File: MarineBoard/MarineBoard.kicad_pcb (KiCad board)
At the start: 4 copper layers, 66.5 x 70 mm, 151 parts, among them CN1 MKDSN 1,5/ 2-5,08, CN2 MKDSN 1,5/ 2-5,08, CN3 SM04B-SRSS-TB (LF)(SN), J1 USB_C_Receptacle_USB2.0_16P, J3 Conn_02x09_Top_Bottom, Q1 IPL60R075CFD7, Q2 S8050, Q3 S8050, U1 SY8089A1AAC, U10 PC817C-S, U11 SN65HVD230DR, U12 DB125-3.5-3P-GN-S, U13 DB125-3.5-3P-GN-S, U14 PC817C-S, U15 TC4427EPA, U16 PC817C-S, U17 PC817C-S, U18 INA226, U19 INA226, U2 INA226, U20 SMAJ6.8CA, U3 TPS5430DDA, U4 DB125-3.5-2P-GN-S, U5 DB125-3.5-2P-GN-S, U6 DB125-3.5-2P-GN-S, U7 DB125-3.5-3P-GN-S, U8 ESP32-S3-WROOM-2-N32R16V, U9 DB125-3.5-3P-GN-S

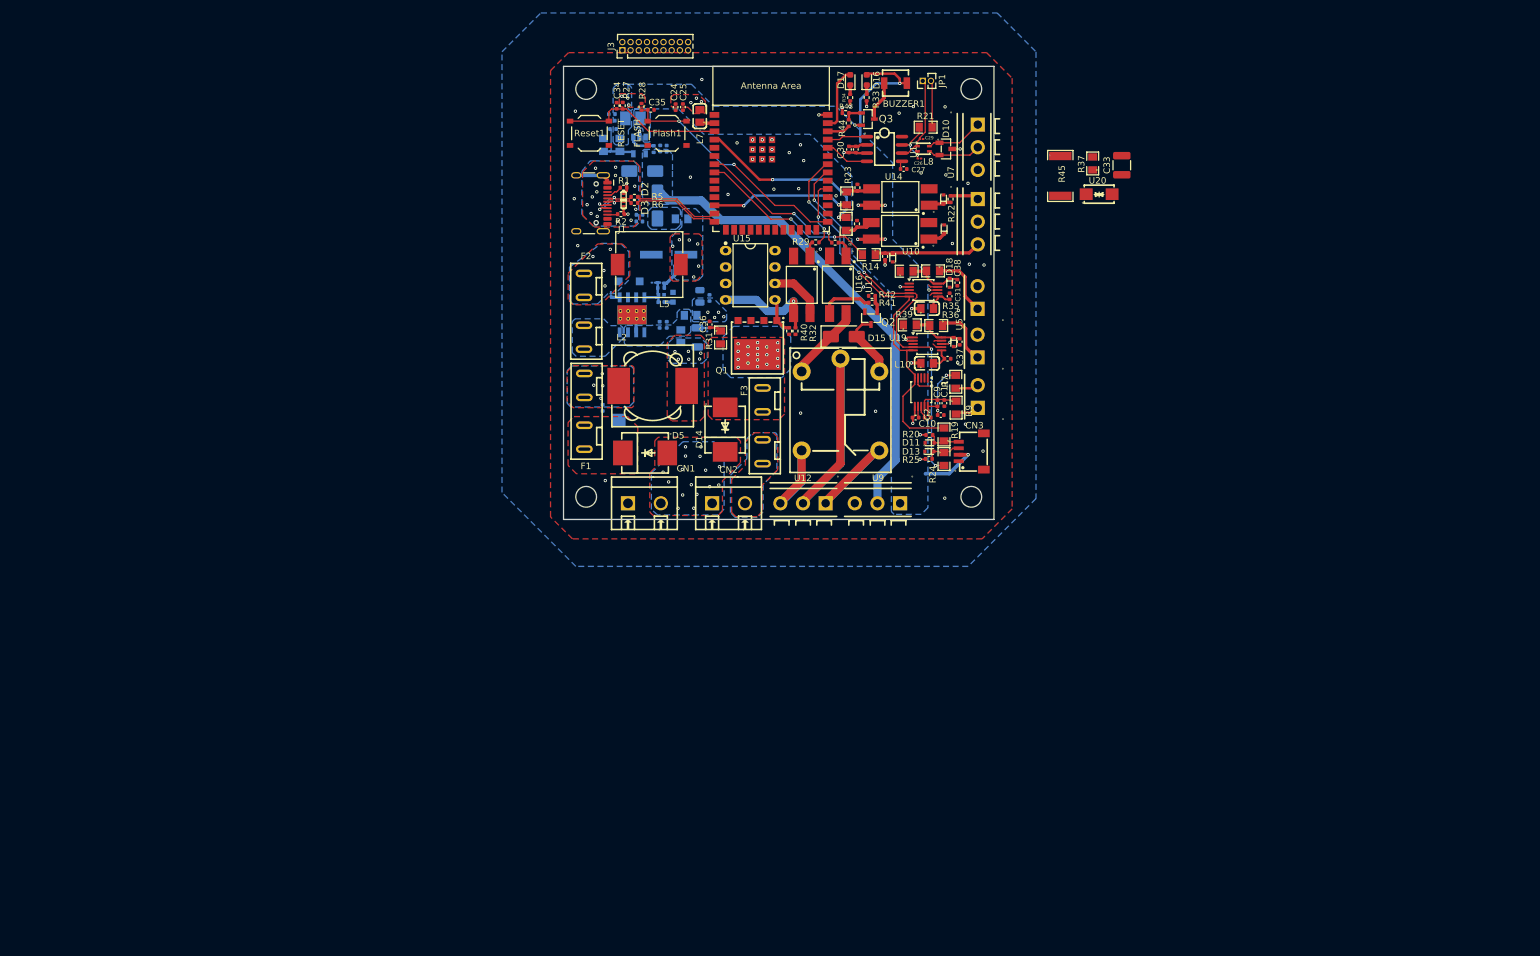
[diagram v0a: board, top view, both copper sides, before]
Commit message: MarineBoard: new from-scratch layout; Quilter-compatible footprints
- LCSC: nickname on all EasyEDA footprint lib IDs (board + schematic)
- EasyEDA.pretty upgraded to current KiCad format; 3D models moved to Lib/Models
- U10 FPC mounting tabs numbered 21/22 to match symbol
- L2 silkscreen arcs replaced with line segments (Quilter parser rejects fp_arc)

Co-Authored-By: Claude Opus 5.5 <noreply@anthropic.com>
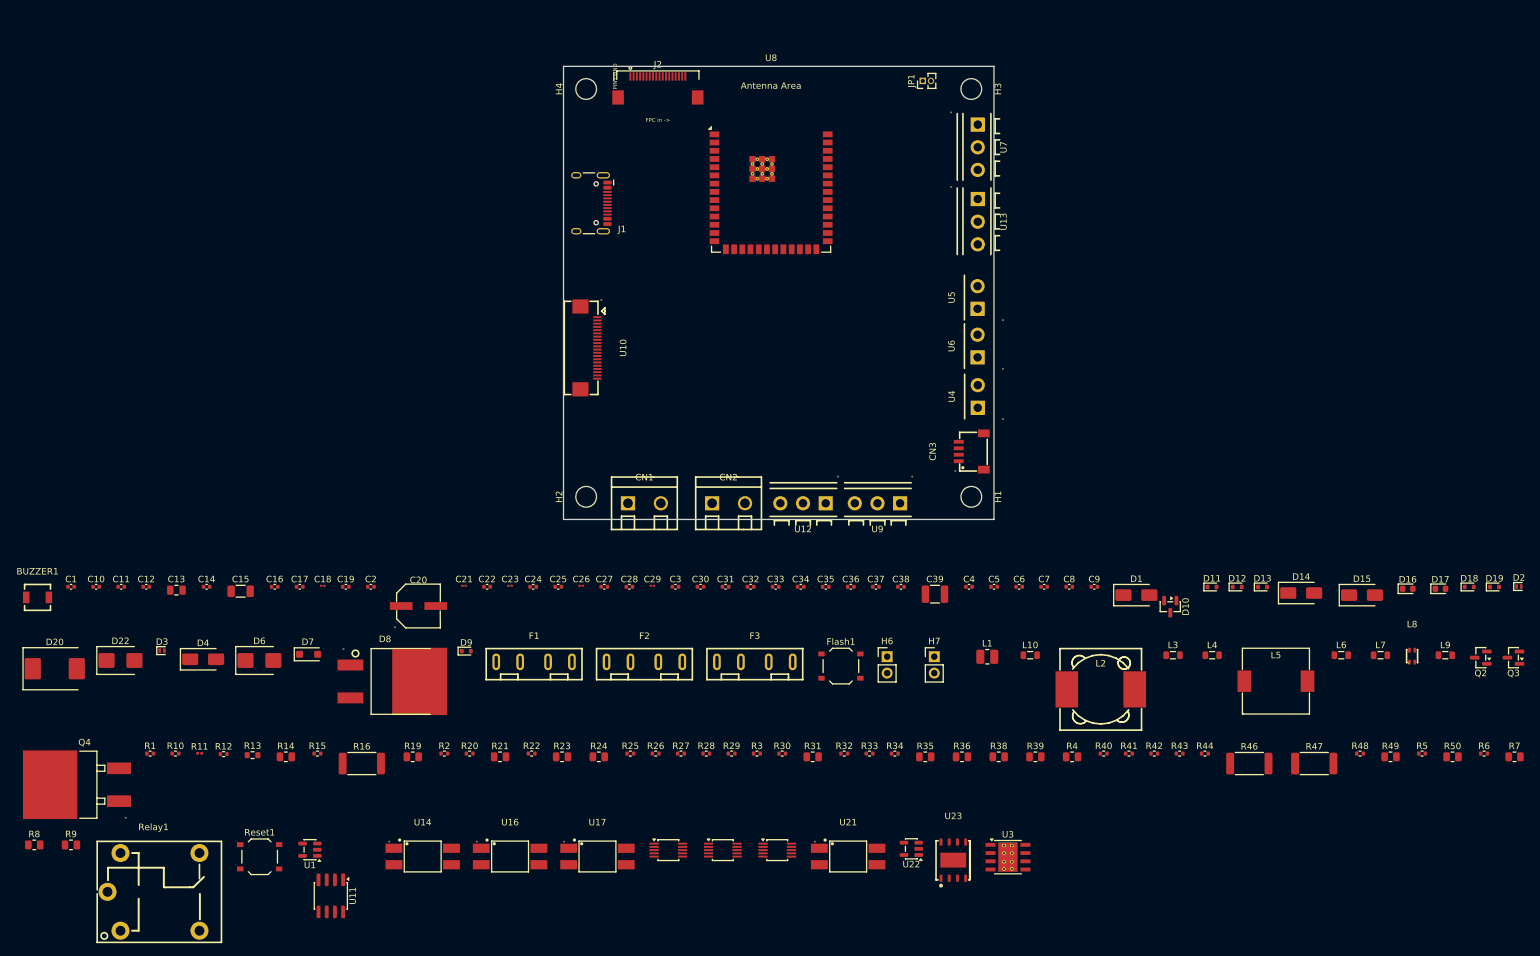
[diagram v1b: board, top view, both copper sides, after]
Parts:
- removed D5: 1N5819HW-7-F, EasyEDA:SMC_L7.1-W6.2-LS8.1-RD
- removed J3: Conn_02x09_Top_Bottom, Connector_PinHeader_1.27mm:PinHeader_2x09_P1.27mm_Vertical
- removed Q1: IPL60R075CFD7, EasyEDA:VSON-4_L8.1-W8.1-P2.00-BL
- removed R17: 120, EasyEDA:R0805
- removed R18: 10K, Resistor_SMD:R_0402_1005Metric
- removed R37: 100K, EasyEDA:R0805
- removed R45: 2K2, EasyEDA:R2512
- removed U15: TC4427EPA, EasyEDA:DIP-8_L9.4-W6.4-P2.54-LS9.1-BL
- removed U20: SMAJ6.8CA, EasyEDA:SMA_L4.4-W2.6-LS5.0-BI
- added C39: 1.2uF 100V, Capacitor_SMD:C_1210_3225Metric, F.Cu at (157.9, 120.0)
- added D20: MBRS3100T3G, Diode_SMD:D_SMC, F.Cu at (21.9, 131.6)
- added D22: S3MB-13-F, Diode_SMD:D_SMB, F.Cu at (32.1, 130.3)
- added H6: MALE HEADER CONNECTOR, Connector_PinHeader_2.54mm:PinHeader_1x02_P2.54mm_Vertical, F.Cu at (150.5, 129.7)
- added H7: MALE HEADER CONNECTOR, Connector_PinHeader_2.54mm:PinHeader_1x02_P2.54mm_Vertical, F.Cu at (157.8, 129.7)
- added J2: DISP_QSPI_4IN_18P, LCSC:FH12-18S-0.5SH_QSPI4IN, F.Cu at (115.1, 41.9)
- added Q4: BUK762R4-60E, LCSC:TO-263-2_L10.1-W9.1-P5.08-LS15.2-BR, F.Cu at (26.5, 149.5)
- added R16: 47K/1W, Resistor_SMD:R_2512_6332Metric, F.Cu at (69.3, 146.2)
- added R46: 47K/1W, Resistor_SMD:R_2512_6332Metric, F.Cu at (206.5, 146.2)
- added R47: 2K2, Resistor_SMD:R_2512_6332Metric, F.Cu at (216.5, 146.2)
- added R48: 10K, Resistor_SMD:R_0402_1005Metric, F.Cu at (223.6, 144.7)
- added R49: 120, Resistor_SMD:R_0805_2012Metric, F.Cu at (228.3, 145.2)
- added R50: 120, Resistor_SMD:R_0805_2012Metric, F.Cu at (237.8, 145.2)
- added U21: PC817C-S, LCSC:SOP-4_L6.5-W4.6-P2.54-LS10.3-TL, F.Cu at (144.5, 160.6)
- added U22: SN74LVC1G14DBVR, Package_TO_SOT_SMD:SOT-23-5, F.Cu at (154.2, 159.4)
- added U23: MCP1407-E/MF_C640313, LCSC:DFN-8_L6.0-W5.0-P1.27-BL-EP4.0, F.Cu at (160.7, 161.1)
- BUZZER1: footprint EasyEDA:BUZ-SMD_L4.0-W4.0-P3.50-L -> LCSC:BUZ-SMD_L4.0-W4.0-P3.50-L
- C1, C13, C14, C15, C16, C17, C18, C19, C21, C22, C23, C3, C4, C5, C6, C7, C8, D1, D4, R10, R3, U3: moved to F.Cu
- C20: footprint EasyEDA:CAP-SMD_BD6.3-L6.6-W6.6-FD -> LCSC:CAP-SMD_BD6.3-L6.6-W6.6-FD; moved to F.Cu
- C33: value 1.2uF 100V -> 4.7uF; footprint Capacitor_SMD:C_1210_3225Metric -> Capacitor_SMD:C_0402_1005Metric
- CN1, CN2: footprint EasyEDA:CONN-TH_2P-P5.08_1729128 -> LCSC:CONN-TH_2P-P5.08_1729128
- CN3: footprint EasyEDA:CONN-SMD_4P-P1.00_SM04B-SRSS-TB-LF-SN -> LCSC:CONN-SMD_4P-P1.00_SM04B-SRSS-TB-LF-SN
- D10: footprint EasyEDA:SOT-23-3_L2.9-W1.3-P1.90-LS2.4-BL-2 -> Package_TO_SOT_SMD:SOT-23
- D11, D12, D13, D18, D19, D9: footprint EasyEDA:SOD-523_L1.2-W0.8-LS1.6-FD -> Diode_SMD:D_SOD-523
- D14: value MURS360T3G -> SS56; footprint EasyEDA:SMC_L7.1-W6.2-LS8.1-R-RD -> Diode_SMD:D_SMA
- D2, D3: footprint EasyEDA:SOD-882_L1.0-W0.6-BI -> Diode_SMD:D_SOD-882
- D6: footprint EasyEDA:SMB_L4.6-W3.6-LS5.3-RD -> Diode_SMD:D_SMB; moved to F.Cu
- D7: footprint EasyEDA:SOD-123FL_L2.7-W1.8-LS3.8-RD -> Diode_SMD:D_SOD-123F; moved to F.Cu
- D8: value ESD5Z3.3T1G -> VS-43CTQ100S-M3; footprint EasyEDA:SOD-523_L1.2-W0.8-LS1.6-FD -> LCSC:D2PAK_L10.0-W9.0-P2.54-LS15.0-TL-1
- F1, F2, F3: footprint EasyEDA:FUSE-TH_XF-506P -> LCSC:FUSE-TH_XF-506P
- J1: footprint EasyEDA:USB_C_Receptacle_HCTL_HC-TYPE-C-16P-01A -> LCSC:USB_C_Receptacle_HCTL_HC-TYPE-C-16P-01A
- L1: footprint EasyEDA:L2520 -> Inductor_SMD:L_1008_2520Metric; moved to F.Cu
- L10, L7, L9: footprint EasyEDA:L0805 -> Inductor_SMD:L_0805_2012Metric
- L2: footprint EasyEDA:IND-SMD_L12.5-W12.5_B82477P4XX -> LCSC:IND-SMD_L12.5-W12.5_B82477P4XX
- L3, L4, L6: footprint EasyEDA:L0805 -> Inductor_SMD:L_0805_2012Metric; moved to F.Cu
- L5: footprint EasyEDA:IND-SMD_L10.2-W10.0 -> LCSC:IND-SMD_L10.2-W10.0
- L8: footprint EasyEDA:FILTER-SMD_4P-L2.0-W1.2-BL_DLW21H -> LCSC:FILTER-SMD_4P-L2.0-W1.2-BL_DLW21H
- Q2, Q3: footprint EasyEDA:SOT-23-3_L2.9-W1.3-P1.90-LS2.3-BR -> Package_TO_SOT_SMD:SOT-23
- R11: footprint EasyEDA:R0201 -> Resistor_SMD:R_0201_0603Metric; moved to F.Cu
- R12: footprint EasyEDA:R0402 -> Resistor_SMD:R_0402_1005Metric; moved to F.Cu
- R13: footprint EasyEDA:R0603 -> Resistor_SMD:R_0603_1608Metric; moved to F.Cu
- R14, R19, R21, R23, R24, R31, R35, R36, R38, R39, R7, R9: footprint EasyEDA:R0805 -> Resistor_SMD:R_0805_2012Metric
- R4, R8: footprint EasyEDA:R0805 -> Resistor_SMD:R_0805_2012Metric; moved to F.Cu
- Relay1: footprint EasyEDA:RELAY-TH_SRD-XXVDC-XL-C -> LCSC:RELAY-TH_SRD-XXVDC-XL-C
- U1: footprint EasyEDA:TSOT-23-5_L2.9-W1.6-P0.95-LS2.8-BR -> Package_TO_SOT_SMD:TSOT-23-5; moved to F.Cu
- U10: value PC817C-S -> 05A20L20P; footprint EasyEDA:SOP-4_L6.5-W4.6-P2.54-LS10.3-TL -> LCSC:FPC-SMD_20P-P0.50_L5.9-W14.4
- U11: footprint EasyEDA:SOIC-8_L5.0-W4.0-P1.27-LS6.0-BL -> Package_SO:SOIC-8_3.9x4.9mm_P1.27mm
- U12, U13, U7, U9: footprint EasyEDA:CONN-TH_3P-P3.50_L7.4-W10.5 -> LCSC:CONN-TH_3P-P3.50_L7.4-W10.5
- U14, U16, U17: footprint EasyEDA:SOP-4_L6.5-W4.6-P2.54-LS10.3-TL -> LCSC:SOP-4_L6.5-W4.6-P2.54-LS10.3-TL
- U18, U19: footprint EasyEDA:VSSOP-10_3x3mm_P0.5mm -> LCSC:VSSOP-10_3x3mm_P0.5mm
- U2: footprint Package_SO:VSSOP-10_3x3mm_P0.5mm -> LCSC:VSSOP-10_3x3mm_P0.5mm
- U4, U5, U6: footprint EasyEDA:CONN-TH_2P-P3.50_L7.4-W7.0 -> LCSC:CONN-TH_2P-P3.50_L7.4-W7.0
- U8: footprint PCM_Espressif:ESP32-S3-WROOM-2 -> RF_Module:ESP32-S3-WROOM-2
- moved R6 156.4 mm to (242.7, 144.7)
- moved BUZZER1 154.5 mm to (19.2, 120.5), turned to 0 degrees
- moved R9 152.5 mm to (24.4, 158.8), turned to 0 degrees
- moved D2 150.9 mm to (248.1, 118.9), turned to 0 degrees
- moved R5 149.0 mm to (233.1, 144.7)
- moved U11 143.6 mm to (64.6, 166.7)
- moved Relay1 139.9 mm to (31.8, 158.0), turned to 0 degrees
- moved R8 139.4 mm to (18.7, 158.8), turned to 0 degrees
- moved L7 134.2 mm to (226.7, 129.5), turned to 0 degrees
- moved C10 131.1 mm to (28.3, 118.9), turned to 0 degrees
- moved C11 130.3 mm to (32.2, 118.9), turned to 0 degrees
- moved Q3 129.9 mm to (247.3, 129.9)
- moved U14 125.8 mm to (78.7, 160.6), turned to 0 degrees
- moved C12 125.6 mm to (36.0, 118.9)
- moved Reset1 122.8 mm to (53.6, 160.6), turned to 0 degrees
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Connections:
- C33 pad 1: SH+ -> GND
- C33 pad 2: Net-(C33-Pad2) -> +12V BAT
- D14 pad 1: PWM1_DRIVE -> Net-(D14-K)
- D8 pad 1: GND -> PWM1_DRIVE
- D8 pad 2: Net-(D8-K) -> +12V BAT
- F1 pad 1: Net-(D5-K) -> Net-(D14-K)
- F2 pad 1: Net-(U3-PH) -> Net-(F2-Pad1)
- F2 pad 2: Net-(D7-C) -> Net-(D4-A)
- L6 pad 2: Net-(D4-A) -> Net-(F2-Pad1)
- U10 pad 1: Net-(D8-K) -> +3.3V
- U10 pad 3: Net-(R17-Pad1) -> FSPICLK/GPIO12
- U10 pad 4: +3.3V -> unconnected-(U10-Pad4)
- U13 pad 2: SH+ -> RPM
- U3 pad 8: Net-(U3-PH) -> Net-(D7-C)
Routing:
- net +5V_VCC: track 72.9 -> 0.00 mm
- net S_GPIO+: track 66.6 -> 0.00 mm, vias 5 -> 0
- net S_GPIO-: track 62.4 -> 0.00 mm, vias 2 -> 0
- net +3.3V: track 54.2 -> 0.00 mm, vias 21 -> 0
- net CO1: track 49.5 -> 0.00 mm
- net BOOT: track 38.2 -> 0.00 mm, vias 2 -> 0
- net RPM_GPIO: track 29.2 -> 0.00 mm, vias 2 -> 0
- net GND: track 28.8 -> 0.00 mm, vias 50 -> 0
- net TMP1_GPIO: track 28.2 -> 0.00 mm, vias 2 -> 0
- net RESET: track 25.4 -> 0.00 mm
- net RLY1_GPIO: track 23.7 -> 0.00 mm, vias 2 -> 0
- net NC1: track 23.6 -> 0.00 mm
- net ENBL_GPIO: track 21.8 -> 0.00 mm, vias 2 -> 0
- net NO1: track 19.0 -> 0.00 mm
- net TMP1: track 16.5 -> 0.00 mm
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- removed copper zone on B.Cu, net +12V
- removed copper zone on In2.Cu, net +12V
- removed copper zone on B.Cu, net +12V BAT
- removed copper zone on F.Cu, net +12V BAT
- removed copper zone on In2.Cu, net +12V BAT
- removed copper zone on B.Cu, net +3.3V
- removed copper zone on F.Cu, net +3.3V
- removed copper zone on B.Cu, net +5V_VCC
- removed copper zone on B.Cu, net GND
- removed copper zone on F.Cu, net GND
- removed copper zone on In1.Cu, net GND
- removed copper zone on In2.Cu, net GND
- removed copper zone on B.Cu, net Net-(C15-Pad1)
- removed copper zone on F.Cu, net Net-(C15-Pad1)
- removed copper zone on B.Cu, net Net-(C20-Pad1)
- removed copper zone on F.Cu, net Net-(C20-Pad1)
- removed copper zone on B.Cu, net Net-(D1-A)
- removed copper zone on F.Cu, net Net-(D1-A)
- removed copper zone on B.Cu, net Net-(D4-A)
- removed copper zone on F.Cu, net Net-(D5-K)
- removed copper zone on B.Cu, net Net-(D6-C)
- removed copper zone on F.Cu, net Net-(D6-C)
- removed copper zone on B.Cu, net Net-(D7-C)
- removed copper zone on F.Cu, net Net-(D7-C)
- removed copper zone on B.Cu, net Net-(U1-LX)
- removed copper zone on B.Cu, net Net-(U3-EN)
- removed copper zone on B.Cu, net Net-(U3-PH)
- removed copper zone on B.Cu, net PWM1
- removed copper zone on F.Cu, net PWM1
- removed copper zone on B.Cu, net PWM1_DRIVE
- removed copper zone on F.Cu, net PWM1_DRIVE
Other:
- board text removed: "+12V"
- board text removed: "12V BAT"
- board text removed: "3.3V"
- board text removed: "5V"
- board text removed: "C01"
- board text removed: "CANH"
- board text removed: "CANL"
- board text removed: "ENBL"
- board text removed: "FLASH"
- board text removed: "GND"
- board text removed: "LVL1"
- board text removed: "LVL2"
- board text removed: "NC1"
- board text removed: "NO1"
- board text removed: "PWM"
- board text removed: "RESET"
- board text removed: "RPM"
- board text removed: "SH+"
- board text removed: "SH-"
- board text removed: "TMP1"

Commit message: MarineBoard: ESP32 decoupling on correct side of ferrite L7
C24/C25 were drawn as the ESP32 decoupling but wired to the +3.3V side of
ferrite bead L7, leaving U8's 3V3 pin with no local capacitance. Rewire them
onto ESP_3V3 (U8 side of L7) and drop the interim C40/C41 duplicates.
C42 (U23 VDD) stays.

Board: saved after Update PCB from Schematic (cap footprint fixes applied);
needs one more F8 to drop C40/C41 and move C24/C25 to ESP_3V3.

Co-Authored-By: Claude Opus 5.5 <noreply@anthropic.com>
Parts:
- added C40: 10uF, Capacitor_SMD:C_0603_1608Metric, F.Cu at (259.3, 122.8)
- added C41: 0.1uF, Capacitor_SMD:C_0402_1005Metric, F.Cu at (258.7, 125.0)
- added C42: 0.1uF, Capacitor_SMD:C_0402_1005Metric, F.Cu at (258.7, 127.0)
- C16, C17: footprint Capacitor_SMD:C_0402_1005Metric -> Capacitor_SMD:C_1206_3216Metric
- C18, C21, C23, C26, C29: footprint Capacitor_SMD:C_01005_0402Metric -> Capacitor_SMD:C_0402_1005Metric
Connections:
- net Net-(U8-3V3) renamed ESP_3V3

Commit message: MarineBoard: board synced to schematic (C24/C25 on ESP_3V3, C40/C41 removed)
DRC schematic parity now 0 issues.

Co-Authored-By: Claude Opus 5.5 <noreply@anthropic.com>
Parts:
- removed C40: 10uF, Capacitor_SMD:C_0603_1608Metric
- removed C41: 0.1uF, Capacitor_SMD:C_0402_1005Metric
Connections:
- C24 pad 2: +3.3V -> ESP_3V3
- C25 pad 1: +3.3V -> ESP_3V3

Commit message: MarineBoard: routed 4-layer board, PCBWay fab package, spec v1.8 (#178)
Board
- Fuses sized to copper: F1 2 A, F3 10 A, new F4 10 A on relay common
- CN2 label fixed (PWM1 vs PWM split left the field open)
- Power nets named; net classes <ROLE>_<V>_<A>; MarineBoard.kicad_dru
  current-width rules + PCBWay-only limits; board rules = stricter of
  project vs PCBWay (clearance 0.127, ring 0.15, hole-to-hole 0.28 ...)
- Edge.Cuts 83.0 x 67.5 mm; duplicate vias removed; GND stitching,
  Q4-source and D8 thermal via arrays; vias moved out of small pads
- U10 (SM10B-GHS-TB) consolidated into Lib/EasyEDA (LCSC lib); stray
  root EasyEDA library removed

Fab / docs
- production/: 4-layer Gerbers + drill + IPC-D-356, zip, BOM, positions
- PCBWay spec sheet: size, ENIG, 1 oz outer, thermal-via plugging note
- Technical Specs v1.8: U10 display header replaces J3/J2/H6/H7,
  Mechanical & fabrication section; Documentation PNGs re-exported
- quilter_nets.py regenerates the Quilter high-current CSV from classes

Co-Authored-By: Claude Opus 5.5 <noreply@anthropic.com>
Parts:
- removed H6, H7: MALE HEADER CONNECTOR, Connector_PinHeader_2.54mm:PinHeader_1x02_P2.54mm_Vertical
- removed J2: DISP_QSPI_4IN_18P, LCSC:FH12-18S-0.5SH_QSPI4IN
- added F4: 10A, LCSC:FUSE-TH_XF-506P, F.Cu at (205.9, 75.5)
- C1, C10, C11, C12, C13, C14, C15, C19, C2, C26, C27, C28, C29, C30, C31, C32, C34, C35, C37, C38, C39, C42, C7, C9, D11, D13, D14, D15, D18, D19, D2, D20, D3, D6, D9, F2, L10, L2, L3, L4, L7, L8, L9, Q2, Q3, R1, R11, R15, R19, R2, R20, R24, R25, R27, R28, R30, R35, R36, R38, R39, R41, R42, R43, R44, R47, R49, R5, R6, R7, R9, U14, U17, U22: moved to B.Cu
- F1: value 5A -> 2A
- F3: value 15A -> 10A
- U10: value 05A20L20P -> SM10B-GHS-TB; footprint LCSC:FPC-SMD_20P-P0.50_L5.9-W14.4 -> LCSC:CONN-SMD_SM10B-GHS-TB; moved to B.Cu
- moved R9 264.2 mm to (270.6, 62.8)
- moved Q4 245.9 mm to (264.8, 88.4), turned to 90 degrees
- moved C10 244.9 mm to (266.2, 60.8), turned to -90 degrees
- moved BUZZER1 244.1 mm to (257.7, 68.2), turned to 180 degrees
- moved C11 242.1 mm to (267.8, 63.3)
- moved C12 236.5 mm to (265.2, 60.8), turned to -90 degrees
- moved U11 228.6 mm to (262.3, 51.8), turned to 0 degrees
- moved R8 220.6 mm to (211.7, 51.8), turned to 180 degrees
- moved Reset1 206.2 mm to (238.4, 69.2), turned to 180 degrees
- moved D20 205.3 mm to (214.4, 60.2)
- moved R19 203.1 mm to (260.2, 57.0), turned to 90 degrees
- moved C2 203.1 mm to (265.8, 62.3)
- moved D22 201.7 mm to (221.8, 62.0), turned to 90 degrees
- moved R21 198.7 mm to (263.9, 47.8), turned to 180 degrees
- moved Relay1 197.9 mm to (214.3, 81.5), turned to -90 degrees
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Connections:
- net FSPICLK/GPIO12 renamed SCK/GPIO12
- net FSPICS0/GPIO10 renamed CS0/GPIO10
- net Net-(C15-Pad1) renamed VIN_FILT
- net Net-(C20-Pad1) renamed 5V_BUCK
- net Net-(D1-A) renamed VBUS
- net Net-(D14-K) renamed VIN_RP
- net Net-(D4-A) renamed 5V_FUSED
- net Net-(D6-C) renamed VIN_FUSED
- net Net-(D7-C) renamed SW_5V
- net Net-(F2-Pad1) renamed 5V_FILT
- net Net-(Q4-G) renamed PWM_GATE
- net Net-(U1-LX) renamed SW_3V3
- net Net-(U3-EN) renamed VIN_BUCK
- net PWM1 renamed PWM
- net PWM1_DRIVE renamed PWM_DRIVE
- Relay1 pad 5: CO1 -> RLY1_COM
- U10 pad 10: unconnected-(U10-Pad10) -> +5V_VCC
- U10 pad 11: unconnected-(U10-Pad11) -> GND
- U10 pad 12: unconnected-(U10-Pad12) -> GND
- U10 pad 4: unconnected-(U10-Pad4) -> MOSI/GPIO11
- U10 pad 5: unconnected-(U10-Pad5) -> MISO/GPIO13
- U10 pad 7: unconnected-(U10-Pad7) -> DC/GPIO9
- U10 pad 8: FSPIRST/GPIO17 -> RST/GPIO14
- U10 pad 9: unconnected-(U10-Pad9) -> BL/GPIO18
- U5 pad 1: LVL1 -> +12V
- U5 pad 2: +12V -> LVL1
- U7 pad 1: CANL -> CANH
- U7 pad 2: CANH -> CANL
- U8 pad 10: FSPIRST/GPIO17 -> unconnected-(U8-GPIO17/U1TXD/ADC2_CH6-Pad10)
- U8 pad 11: FSPIBL/GPIO18 -> BL/GPIO18
- U8 pad 15: GPIO3 -> unconnected-(U8-GPIO3/TOUCH3/ADC1_CH2-Pad15)
- U8 pad 17: FSPIHD/GPIO9 -> DC/GPIO9
- U8 pad 19: FSPID/GPIO11 -> MOSI/GPIO11
- U8 pad 21: FSPIQ/GPIO13 -> MISO/GPIO13
- U8 pad 22: FSPIWP/GPIO14 -> RST/GPIO14
- U8 pad 23: FSPIDC/GPIO21 -> unconnected-(U8-GPIO21-Pad23)
- U8 pad 24: FSPITI/GPIO47 -> unconnected-(U8-GPIO47/SPICLK_P/SUBSPICLK_P_DIFF-Pad24)
- U8 pad 32: FSPICS1/GPIO39 -> unconnected-(U8-MTCK/GPIO39/CLK_OUT3/SUBSPICS1-Pad32)
- U8 pad 35: FSPITE/GPIO42 -> unconnected-(U8-MTMS/GPIO42-Pad35)
- U8 pad 5: GPIO5 -> unconnected-(U8-GPIO5/TOUCH5/ADC1_CH4-Pad5)
- U8 pad 6: GPIO6 -> unconnected-(U8-GPIO6/TOUCH6/ADC1_CH5-Pad6)
- U8 pad 9: GPIO16 -> unconnected-(U8-GPIO16/U0CTS/ADC2_CH5/XTAL_32K_N-Pad9)
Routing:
- net +5V_VCC: track 0.00 -> 93.7 mm, vias 0 -> 5
- net RLY1_GPIO: track 0.00 -> 58.1 mm, vias 0 -> 3
- net S_GPIO+: track 0.00 -> 43.5 mm, vias 0 -> 6
- net ENBL_GPIO: track 0.00 -> 40.9 mm, vias 0 -> 4
- net +3.3V: track 0.00 -> 40.8 mm, vias 0 -> 23
- net USB_D+: track 0.00 -> 39.4 mm, vias 0 -> 1
- net S_GPIO-: track 0.00 -> 38.7 mm, vias 0 -> 4
- net USB_D-: track 0.00 -> 38.5 mm, vias 0 -> 1
- net TMP1_GPIO: track 0.00 -> 35.7 mm, vias 0 -> 2
- net LED: track 0.00 -> 29.8 mm
- net RESET: track 0.00 -> 27.2 mm, vias 0 -> 1
- net 5V_BUCK: track 0.00 -> 25.9 mm
- net PWM1_GPIO: track 0.00 -> 24.4 mm
- net BUZZ: track 0.00 -> 20.7 mm, vias 0 -> 1
- net +12V BAT: track 0.00 -> 20.6 mm, vias 0 -> 65
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- added copper zone on In2.Cu, net +12V
- added copper zone on B.Cu, net +12V BAT
- added copper zone on F.Cu, net +12V BAT
- added copper zone on In2.Cu, net +12V BAT
- added copper zone on F.Cu, net +3.3V
- added copper zone on In2.Cu, net +3.3V
- added copper zone on F.Cu, net +5V_VCC
- added copper zone on F.Cu, net 5V_BUCK
- added copper zone on F.Cu, net CO1
- added copper zone on B.Cu, net GND
- added copper zone on F.Cu, net GND
- added copper zone on In1.Cu, net GND
- added copper zone on F.Cu, net NC1
- added copper zone on F.Cu, net NO1
- added copper zone on F.Cu, net Net-(U1-FB)
- added copper zone on F.Cu, net Net-(U3-VSENSE)
- added copper zone on F.Cu, net PWM
- added copper zone on In2.Cu, net PWM
- added copper zone on F.Cu, net PWM_DRIVE
- added copper zone on In2.Cu, net PWM_DRIVE
- added copper zone on F.Cu, net RLY1_COM
- added copper zone on F.Cu, net SW_3V3
- added copper zone on F.Cu, net SW_5V
- added copper zone on F.Cu, net VIN_BUCK
- added copper zone on B.Cu, net VIN_FUSED
- added copper zone on B.Cu, net VIN_RP
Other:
- board size 66.5 x 70 mm -> 83 x 67.5 mm
